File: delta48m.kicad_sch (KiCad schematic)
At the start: 0 parts

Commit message: 20 march version
Added 2nd list, working on the third
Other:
- added sheet Logic (logic.kicad_sch)

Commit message: March 23rd Update 1
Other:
- added sheet Video (video.kicad_sch)
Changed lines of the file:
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@@
+    )
+  )
+  (sheet (at 33.655 97.79) (size 46.355 38.1) (fields_autoplaced)
+    (stroke (width 0.1524) (type solid) (color 0 0 0 0))
+    (fill (color 0 0 0 0.0000))
+    (property "Sheet name" "Video" (id 0) (at 33.655 97.0784 0)
+      (effects (font (size 1.27 1.27)) (justify left bottom))
+    )
+    (property "Sheet file" "video.kicad_sch" (id 1) (at 33.655 136.4746 0)
+      (effects (font (size 1.27 1.27)) (justify left top))
     )
   )
@@
     (path "/f8af5ff9-7e59-42c3-8772-58b22d974813" (page "9"))
     (path "/f4495deb-4b48-4c40-8488-ac0dd7ca5eeb" (page "10"))
+    (path "/65352eb4-688f-4c08-b5e4-ec3cc93bd7c5" (page "11"))
   )
   (symbol_instances
@@
       (reference "#PWR0242") (unit 1) (value "GND") (footprint "")
     )
+    (path "/65352eb4-688f-4c08-b5e4-ec3cc93bd7c5/2c8c1792-6f45-4750-afc0-0b9456af4b0b"
+      (reference "#PWR?") (unit 1) (value "GND") (footprint "")
+    )
+    (path "/65352eb4-688f-4c08-b5e4-ec3cc93bd7c5/3db1a6a3-fa9a-4237-b821-de3326c85149"
+      (reference "#PWR?") (unit 1) (value "+5V") (footprint "")
+    )
     (path "/f4495deb-4b48-4c40-8488-ac0dd7ca5eeb/e2a4a70d-e8be-44e4-9449-0cdaa719531d"
       (reference "C1") (unit 1) (value "120pF") (footprint "")
@@
       (reference "JP3") (unit 1) (value "Jumper_2_Open") (footprint "Connector_PinHeader_2.54mm:PinHeader_1x02_P2.54mm_Vertical")
     )
+    (path "/65352eb4-688f-4c08-b5e4-ec3cc93bd7c5/4ff3d2ef-10f2-46d3-910b-d3d7f689fb43"
+      (reference "LS?") (unit 1) (value "Speaker") (footprint "")
+    )
+    (path "/65352eb4-688f-4c08-b5e4-ec3cc93bd7c5/28ff482f-1a93-45b9-b3e6-da77c208dceb"
+      (reference "Q1") (unit 1) (value "BC547B") (footprint "Package_TO_SOT_THT:TO-92_Inline")
+    )
+    (path "/65352eb4-688f-4c08-b5e4-ec3cc93bd7c5/3e2d5224-89c2-46e4-ae22-0f9b946d4c7f"
+      (reference "Q3") (unit 1) (value "BC547B") (footprint "Package_TO_SOT_THT:TO-92_Inline")
+    )
+    (path "/65352eb4-688f-4c08-b5e4-ec3cc93bd7c5/f2667019-1db0-4f75-897c-633c9c4a6ab0"
+      (reference "Q4") (unit 1) (value "BC547B") (footprint "Package_TO_SOT_THT:TO-92_Inline")
+    )
+    (path "/65352eb4-688f-4c08-b5e4-ec3cc93bd7c5/d4220a21-5aaf-4fdd-8dc6-f9d9a52f1a09"
+      (reference "Q5") (unit 1) (value "BC547B") (footprint "Package_TO_SOT_THT:TO-92_Inline")
+    )
+    (path "/65352eb4-688f-4c08-b5e4-ec3cc93bd7c5/e13fbdfe-57f8-4af0-b9a4-32c1458a6ab9"
+      (reference "Q6") (unit 1) (value "BC547B") (footprint "Package_TO_SOT_THT:TO-92_Inline")
+    )
     (path "/f4495deb-4b48-4c40-8488-ac0dd7ca5eeb/2cc738a6-8c10-4108-be9c-ad025694bc7e"
       (reference "R1") (unit 1) (value "470") (footprint "")
@@
       (reference "R23") (unit 1) (value "240") (footprint "")
     )
+    (path "/65352eb4-688f-4c08-b5e4-ec3cc93bd7c5/2240d07f-dd5e-4723-9b01-bffa5bc06a0d"
+      (reference "R24") (unit 1) (value "R") (footprint "")
+    )
+    (path "/65352eb4-688f-4c08-b5e4-ec3cc93bd7c5/54ca4ed2-c9a2-486c-a1ce-f5334567ec0f"
+      (reference "R25") (unit 1) (value "R") (footprint "")
+    )
+    (path "/65352eb4-688f-4c08-b5e4-ec3cc93bd7c5/96158b35-c74d-4722-b283-e45154b67890"
+      (reference "R26") (unit 1) (value "R") (footprint "")
+    )
+    (path "/65352eb4-688f-4c08-b5e4-ec3cc93bd7c5/48046ebd-58fe-4ee5-93a2-6a7eb33338c3"
+      (reference "R28") (unit 1) (value "R") (footprint "")
+    )
+    (path "/65352eb4-688f-4c08-b5e4-ec3cc93bd7c5/cdcfe811-df37-480d-bb3d-11af89d3051b"
+      (reference "R30") (unit 1) (value "R") (footprint "")
+    )
     (path "/f8af5ff9-7e59-42c3-8772-58b22d974813/050e9f11-84c5-4281-bf7f-9b0fe553a597"
       (reference "R32") (unit 1) (value "470") (footprint "")
     )
+    (path "/65352eb4-688f-4c08-b5e4-ec3cc93bd7c5/c80a08ff-2dcb-4747-b223-e8a69e94b014"
+      (reference "R33") (unit 1) (value "R") (footprint "")
+    )
     (path "/f8af5ff9-7e59-42c3-8772-58b22d974813/b9746cc7-02ec-423c-9297-43c12de5374e"
       (reference "R34") (unit 1) (value "2.7K") (footprint "")
@@
       (reference "R36") (unit 1) (value "470") (footprint "")
     )
-    (path "/f8af5ff9-7e59-42c3-8772-58b22d974813/d5752059-0b53-404a-8a15-bc3d49aa65b0"
+    (path "/65352eb4-688f-4c08-b5e4-ec3cc93bd7c5/3df5d887-787c-464e-9b4b-6f6e12f725c1"
       (reference "R37") (unit 1) (value "1.5K") (footprint "")
     )
@@
       (reference "R39") (unit 1) (value "470") (footprint "")
     )
-    (path "/f8af5ff9-7e59-42c3-8772-58b22d974813/656aec00-443e-4726-8ec1-21ad34c42cd7"
+    (path "/65352eb4-688f-4c08-b5e4-ec3cc93bd7c5/3d32dd0f-af7c-48fa-9b91-a566b81d0408"
       (reference "R40") (unit 1) (value "5.6K") (footprint "")
     )
@@
       (reference "R53") (unit 1) (value "510") (footprint "")
     )
+    (path "/65352eb4-688f-4c08-b5e4-ec3cc93bd7c5/e1eb92c4-a816-4d58-a500-d113005315f4"
+      (reference "R?") (unit 1) (value "R") (footprint "")
+    )
+    (path "/65352eb4-688f-4c08-b5e4-ec3cc93bd7c5/05fe21a0-7bca-434b-90a5-f634c3136997"
+      (reference "RV42") (unit 1) (value "R_Potentiometer") (footprint "")
+    )
+    (path "/65352eb4-688f-4c08-b5e4-ec3cc93bd7c5/37718f15-012d-4a23-8f29-c0dfb28415be"
+      (reference "RV43") (unit 1) (value "R_Potentiometer") (footprint "")
+    )
+    (path "/65352eb4-688f-4c08-b5e4-ec3cc93bd7c5/ec53dd31-bcda-49e3-9ac1-6753c5b8c95b"
+      (reference "RV44") (unit 1) (value "R_Potentiometer") (footprint "")
+    )
     (path "/f4495deb-4b48-4c40-8488-ac0dd7ca5eeb/8f8eeb4a-48cf-4f29-9a36-8fb6d2f379c4"

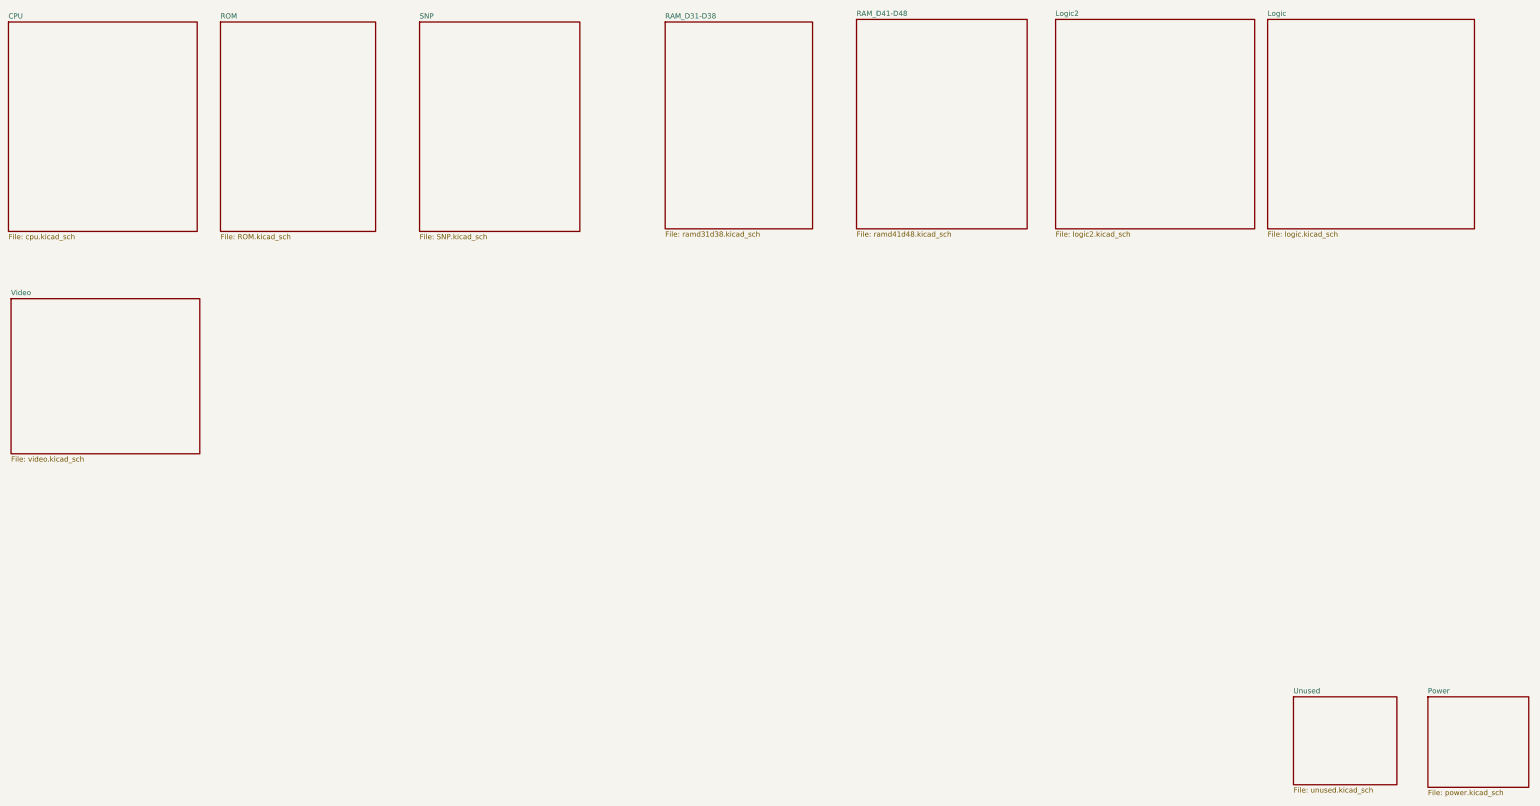
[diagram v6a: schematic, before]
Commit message: March 23rd First pre-alpha
First time ZERO errors and 93 warnings. Schematics are done, now to deal with warnings and footprints.
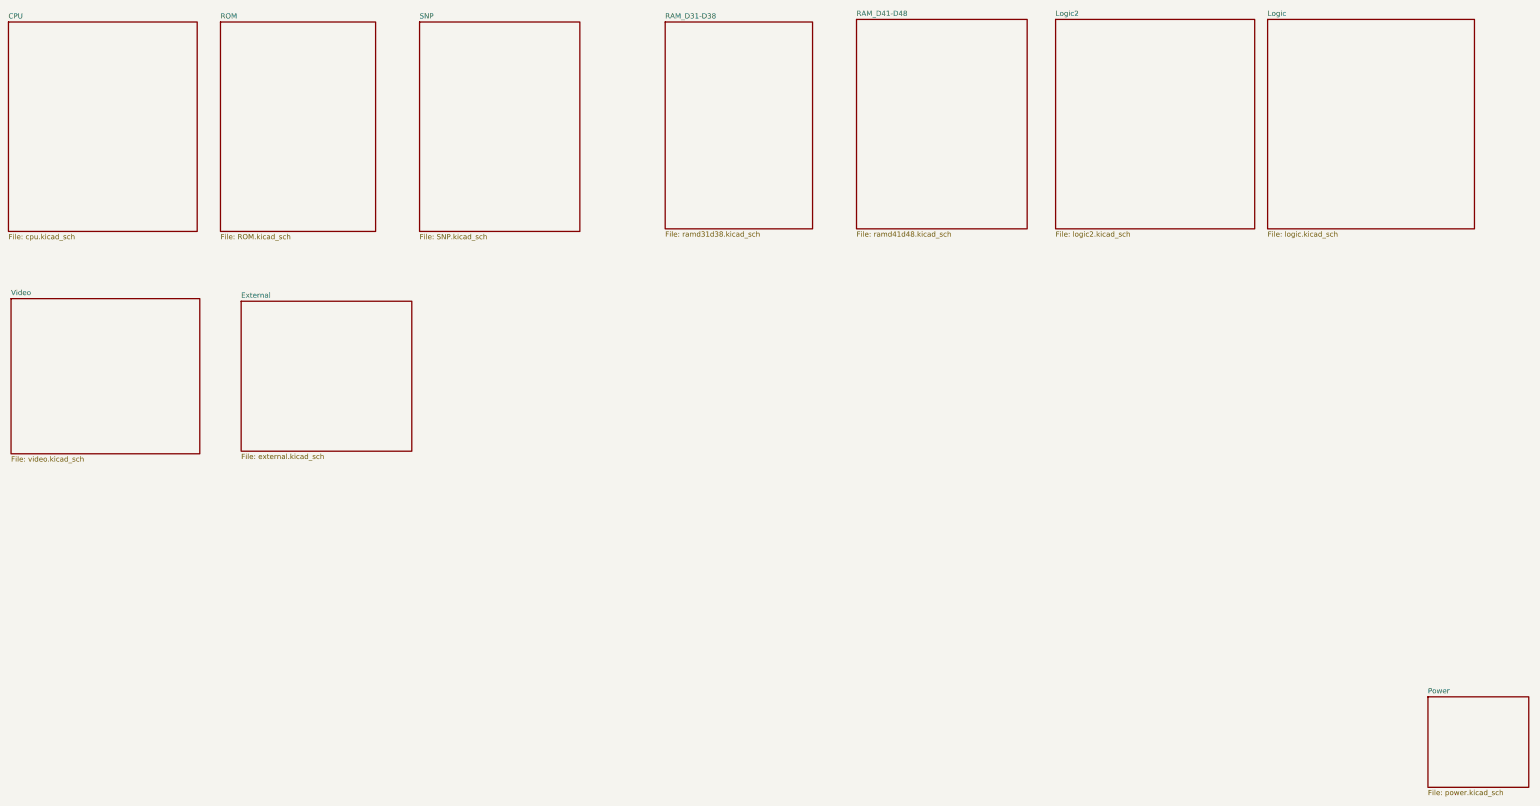
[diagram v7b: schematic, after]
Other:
- removed sheet Unused
- added sheet External (external.kicad_sch)
